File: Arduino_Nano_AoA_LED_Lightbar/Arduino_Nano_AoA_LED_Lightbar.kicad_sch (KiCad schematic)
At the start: 17 parts, among them J1 Conn_01x09_Pin

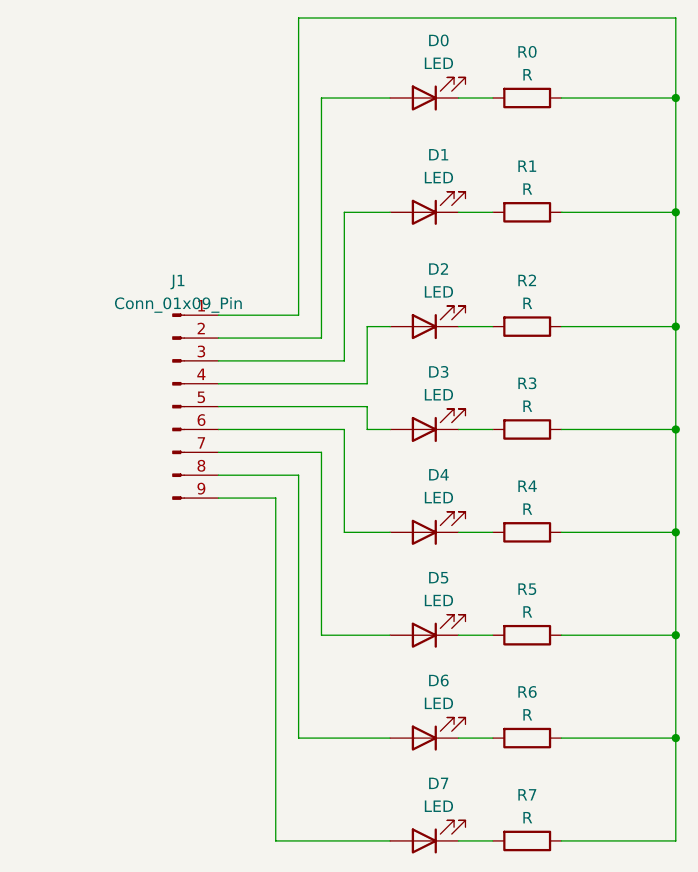
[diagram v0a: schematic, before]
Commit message: Created a new board for the Wit-Motion WT901B IMU chip.
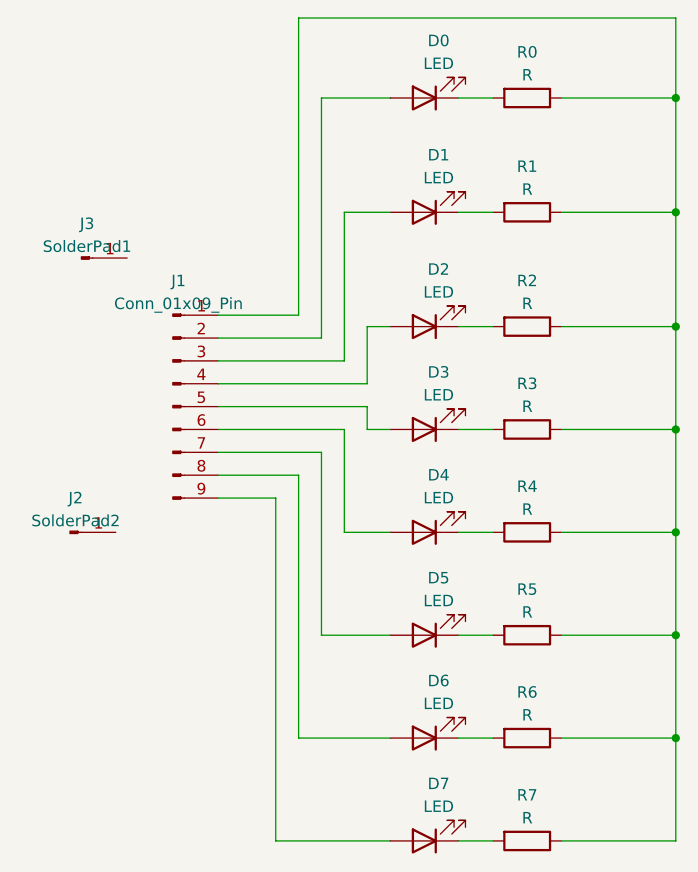
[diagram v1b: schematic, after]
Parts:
- added J2: SolderPad2, TestPoint:TestPoint_Pad_D4.0mm, symbol Connector:Conn_01x01_Pin
- added J3: SolderPad1, TestPoint:TestPoint_Pad_D4.0mm, symbol Connector:Conn_01x01_Pin
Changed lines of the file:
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@@
+    )
+  )
+  (symbol (lib_id "Connector:Conn_01x01_Pin") (at 90.17 69.85 0) (unit 1)
+    (in_bom yes) (on_board yes) (dnp no) (fields_autoplaced)
+    (property "Reference" "J3" (at 90.805 66.04 0)
+      (effects (font (size 1.27 1.27)))
+    )
+    (property "Value" "SolderPad1" (at 90.805 68.58 0)
+      (effects (font (size 1.27 1.27)))
+    )
+    (property "Footprint" "TestPoint:TestPoint_Pad_D4.0mm" (at 90.17 69.85 0)
+      (effects (font (size 1.27 1.27)) hide)
+    )
+    (property "Datasheet" "~" (at 90.17 69.85 0)
+      (effects (font (size 1.27 1.27)) hide)
+    )
+    (pin "1")
+    (instances
+      (project "Arduino_Nano_AoA_LED_Lightbar"
+        (path "/6d661427-1f51-4d30-8fab-bdd339673842"
+          (reference "J3") (unit 1)
+        )
+      )
     )
   )
@@
         )
       )
+    )
+  )
+  (symbol (lib_id "Connector:Conn_01x01_Pin") (at 88.9 100.33 0) (unit 1)
+    (in_bom yes) (on_board yes) (dnp no) (fields_autoplaced)
+    (property "Reference" "J2" (at 89.535 96.52 0)
+      (effects (font (size 1.27 1.27)))
+    )
+    (property "Value" "SolderPad2" (at 89.535 99.06 0)
+      (effects (font (size 1.27 1.27)))
+    )
+    (property "Footprint" "TestPoint:TestPoint_Pad_D4.0mm" (at 88.9 100.33 0)
+      (effects (font (size 1.27 1.27)) hide)
+    )
+    (property "Datasheet" "~" (at 88.9 100.33 0)
+      (effects (font (size 1.27 1.27)) hide)
+    )
+    (pin "1")
+    (instances
+      (project "Arduino_Nano_AoA_LED_Lightbar"
+        (path "/6d661427-1f51-4d30-8fab-bdd339673842"
+          (reference "J2") (unit 1)
+        )
+      )
